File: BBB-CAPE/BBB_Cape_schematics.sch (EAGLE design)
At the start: 81 parts, among them IC1 EEPROM-I2CSMD, SW1 219-02, SW2 219-02

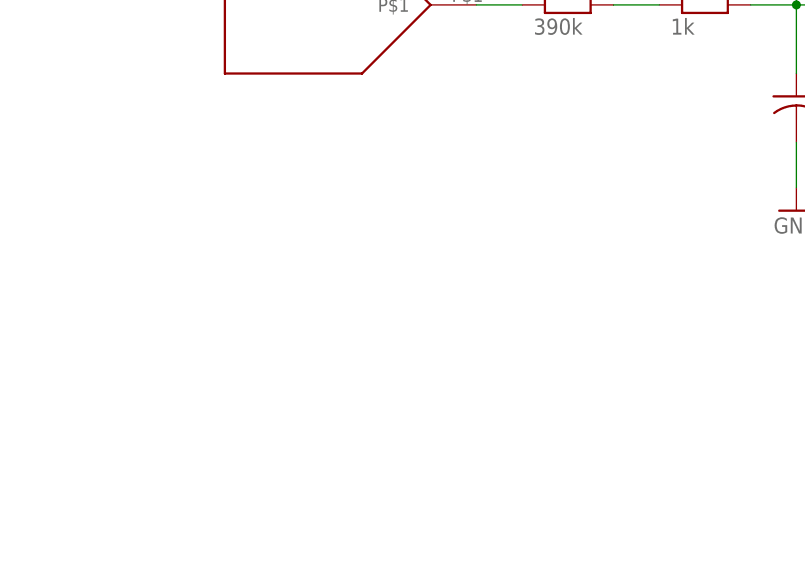
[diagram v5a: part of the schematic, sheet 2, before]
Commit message: Add ground pad(for index finger) in BBB_Cape_schematics.sch
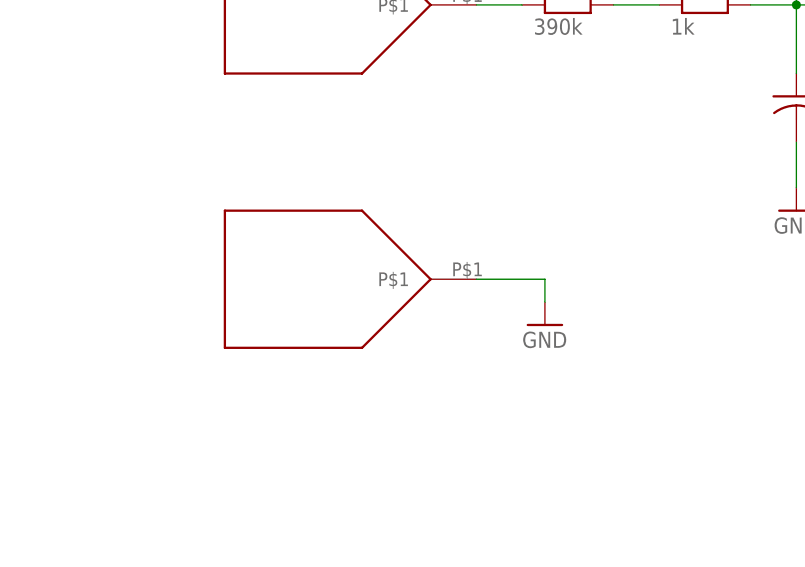
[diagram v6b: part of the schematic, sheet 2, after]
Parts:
- added U$24: PAD, Components:PAD
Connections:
- net GND: now also U$24.P$1
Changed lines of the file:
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@@
 <grid distance="0.1" unitdist="inch" unit="inch" style="lines" multiple="1" display="yes" altdistance="0.01" altunitdist="inch" altunit="inch"/>
 <layers>
-<layer number="1" name="Top" color="4" fill="1" visible="yes" active="no"/>
-<layer number="2" name="Route2" color="1" fill="3" visible="yes" active="no"/>
-<layer number="3" name="Route3" color="4" fill="3" visible="yes" active="no"/>
-<layer number="4" name="Route4" color="1" fill="4" visible="yes" active="no"/>
-<layer number="5" name="Route5" color="4" fill="4" visible="yes" active="no"/>
-<layer number="6" name="Route6" color="1" fill="8" visible="yes" active="no"/>
-<layer number="7" name="Route7" color="4" fill="8" visible="yes" active="no"/>
-<layer number="8" name="Route8" color="1" fill="2" visible="yes" active="no"/>
-<layer number="9" name="Route9" color="4" fill="2" visible="yes" active="no"/>
-<layer number="10" name="Route10" color="1" fill="7" visible="yes" active="no"/>
-<layer number="11" name="Route11" color="4" fill="7" visible="yes" active="no"/>
-<layer number="12" name="Route12" color="1" fill="5" visible="yes" active="no"/>
-<layer number="13" name="Route13" color="4" fill="5" visible="yes" active="no"/>
-<layer number="14" name="Route14" color="1" fill="6" visible="yes" active="no"/>
-<layer number="15" name="Route15" color="4" fill="6" visible="yes" active="no"/>
-<layer number="16" name="Bottom" color="1" fill="1" visible="yes" active="no"/>
-<layer number="17" name="Pads" color="2" fill="1" visible="yes" active="no"/>
-<layer number="18" name="Vias" color="2" fill="1" visible="yes" active="no"/>
-<layer number="19" name="Unrouted" color="6" fill="1" visible="yes" active="no"/>
-<layer number="20" name="Dimension" color="15" fill="1" visible="yes" active="no"/>
-<layer number="21" name="tPlace" color="7" fill="1" visible="yes" active="no"/>
-<layer number="22" name="bPlace" color="7" fill="1" visible="yes" active="no"/>
-<layer number="23" name="tOrigins" color="15" fill="1" visible="yes" active="no"/>
-<layer number="24" name="bOrigins" color="15" fill="1" visible="yes" active="no"/>
-<layer number="25" name="tNames" color="7" fill="1" visible="yes" active="no"/>
-<layer number="26" name="bNames" color="7" fill="1" visible="yes" active="no"/>
-<layer number="27" name="tValues" color="7" fill="1" visible="yes" active="no"/>
-<layer number="28" name="bValues" color="7" fill="1" visible="yes" active="no"/>
+<layer number="1" name="Top" color="4" fill="1" visible="no" active="no"/>
+<layer number="2" name="Route2" color="1" fill="3" visible="no" active="no"/>
+<layer number="3" name="Route3" color="4" fill="3" visible="no" active="no"/>
+<layer number="4" name="Route4" color="1" fill="4" visible="no" active="no"/>
+<layer number="5" name="Route5" color="4" fill="4" visible="no" active="no"/>
+<layer number="6" name="Route6" color="1" fill="8" visible="no" active="no"/>
+<layer number="7" name="Route7" color="4" fill="8" visible="no" active="no"/>
+<layer number="8" name="Route8" color="1" fill="2" visible="no" active="no"/>
+<layer number="9" name="Route9" color="4" fill="2" visible="no" active="no"/>
+<layer number="10" name="Route10" color="1" fill="7" visible="no" active="no"/>
+<layer number="11" name="Route11" color="4" fill="7" visible="no" active="no"/>
+<layer number="12" name="Route12" color="1" fill="5" visible="no" active="no"/>
+<layer number="13" name="Route13" color="4" fill="5" visible="no" active="no"/>
+<layer number="14" name="Route14" color="1" fill="6" visible="no" active="no"/>
+<layer number="15" name="Route15" color="4" fill="6" visible="no" active="no"/>
+<layer number="16" name="Bottom" color="1" fill="1" visible="no" active="no"/>
+<layer number="17" name="Pads" color="2" fill="1" visible="no" active="no"/>
+<layer number="18" name="Vias" color="2" fill="1" visible="no" active="no"/>
+<layer number="19" name="Unrouted" color="6" fill="1" visible="no" active="no"/>
+<layer number="20" name="Dimension" color="15" fill="1" visible="no" active="no"/>
+<layer number="21" name="tPlace" color="7" fill="1" visible="no" active="no"/>
+<layer number="22" name="bPlace" color="7" fill="1" visible="no" active="no"/>
+<layer number="23" name="tOrigins" color="15" fill="1" visible="no" active="no"/>
+<layer number="24" name="bOrigins" color="15" fill="1" visible="no" active="no"/>
+<layer number="25" name="tNames" color="7" fill="1" visible="no" active="no"/>
+<layer number="26" name="bNames" color="7" fill="1" visible="no" active="no"/>
+<layer number="27" name="tValues" color="7" fill="1" visible="no" active="no"/>
+<layer number="28" name="bValues" color="7" fill="1" visible="no" active="no"/>
 <layer number="29" name="tStop" color="7" fill="3" visible="no" active="no"/>
 <layer number="30" name="bStop" color="7" fill="6" visible="no" active="no"/>
@@
 <layer number="35" name="tGlue" color="7" fill="4" visible="no" active="no"/>
 <layer number="36" name="bGlue" color="7" fill="5" visible="no" active="no"/>
-<layer number="37" name="tTest" color="7" fill="1" visible="yes" active="no"/>
-<layer number="38" name="bTest" color="7" fill="1" visible="yes" active="no"/>
+<layer number="37" name="tTest" color="7" fill="1" visible="no" active="no"/>
+<layer number="38" name="bTest" color="7" fill="1" visible="no" active="no"/>
 <layer number="39" name="tKeepout" color="4" fill="11" visible="no" active="no"/>
 <layer number="40" name="bKeepout" color="1" fill="11" visible="no" active="no"/>
@@
 <layer number="44" name="Drills" color="7" fill="1" visible="no" active="no"/>
 <layer number="45" name="Holes" color="7" fill="1" visible="no" active="no"/>
-<layer number="46" name="Milling" color="3" fill="1" visible="yes" active="no"/>
-<layer number="47" name="Measures" color="7" fill="1" visible="yes" active="no"/>
-<layer number="48" name="Document" color="7" fill="1" visible="yes" active="no"/>
-<layer number="49" name="Reference" color="7" fill="1" visible="yes" active="no"/>
-<layer number="50" name="dxf" color="7" fill="1" visible="yes" active="no"/>
-<layer number="51" name="tDocu" color="7" fill="1" visible="yes" active="no"/>
-<layer number="52" name="bDocu" color="7" fill="1" visible="yes" active="no"/>
-<layer number="53" name="tGND_GNDA" color="7" fill="9" visible="yes" active="no"/>
-<layer number="54" name="bGND_GNDA" color="1" fill="9" visible="yes" active="no"/>
-<layer number="56" name="wert" color="7" fill="1" visible="yes" active="no"/>
+<layer number="46" name="Milling" color="3" fill="1" visible="no" active="no"/>
+<layer number="47" name="Measures" color="7" fill="1" visible="no" active="no"/>
+<layer number="48" name="Document" color="7" fill="1" visible="no" active="no"/>
+<layer number="49" name="Reference" color="7" fill="1" visible="no" active="no"/>
+<layer number="50" name="dxf" color="7" fill="1" visible="no" active="no"/>
+<layer number="51" name="tDocu" color="7" fill="1" visible="no" active="no"/>
+<layer number="52" name="bDocu" color="7" fill="1" visible="no" active="no"/>
+<layer number="53" name="tGND_GNDA" color="7" fill="9" visible="no" active="no"/>
+<layer number="54" name="bGND_GNDA" color="1" fill="9" visible="no" active="no"/>
+<layer number="56" name="wert" color="7" fill="1" visible="no" active="no"/>
 <layer number="91" name="Nets" color="2" fill="1" visible="yes" active="yes"/>
 <layer number="92" name="Busses" color="1" fill="1" visible="yes" active="yes"/>
@@
 <part name="SW1" library="switch-dil" deviceset="219-02*" device=""/>
 <part name="SW2" library="switch-dil" deviceset="219-02*" device=""/>
+<part name="U$24" library="Components" deviceset="PAD" device=""/>
+<part name="GND28" library="supply1" deviceset="GND" device=""/>
 </parts>
 <sheets>
@@
 <attribute name="VALUE" x="334.264" y="220.091" size="1.778" layer="96" rot="R180"/>
 </instance>
+<instance part="U$24" gate="G$1" x="68.58" y="139.7"/>
+<instance part="GND28" gate="1" x="93.98" y="134.62"/>
 </instances>
 <busses>
@@
 <wire x1="195.58" y1="137.16" x2="195.58" y2="134.62" width="0.1524" layer="91"/>
 </segment>
-</net>
+<segment>
+<pinref part="U$24" gate="G$1" pin="P$1"/>
+<wire x1="86.36" y1="139.7" x2="93.98" y2="139.7" width="0.1524" layer="91"/>
+<pinref part="GND28" gate="1" pin="GND"/>
+<wire x1="93.98" y1="139.7" x2="93.98" y2="137.16" width="0.1524" layer="91"/>
+</segment>
+</net>

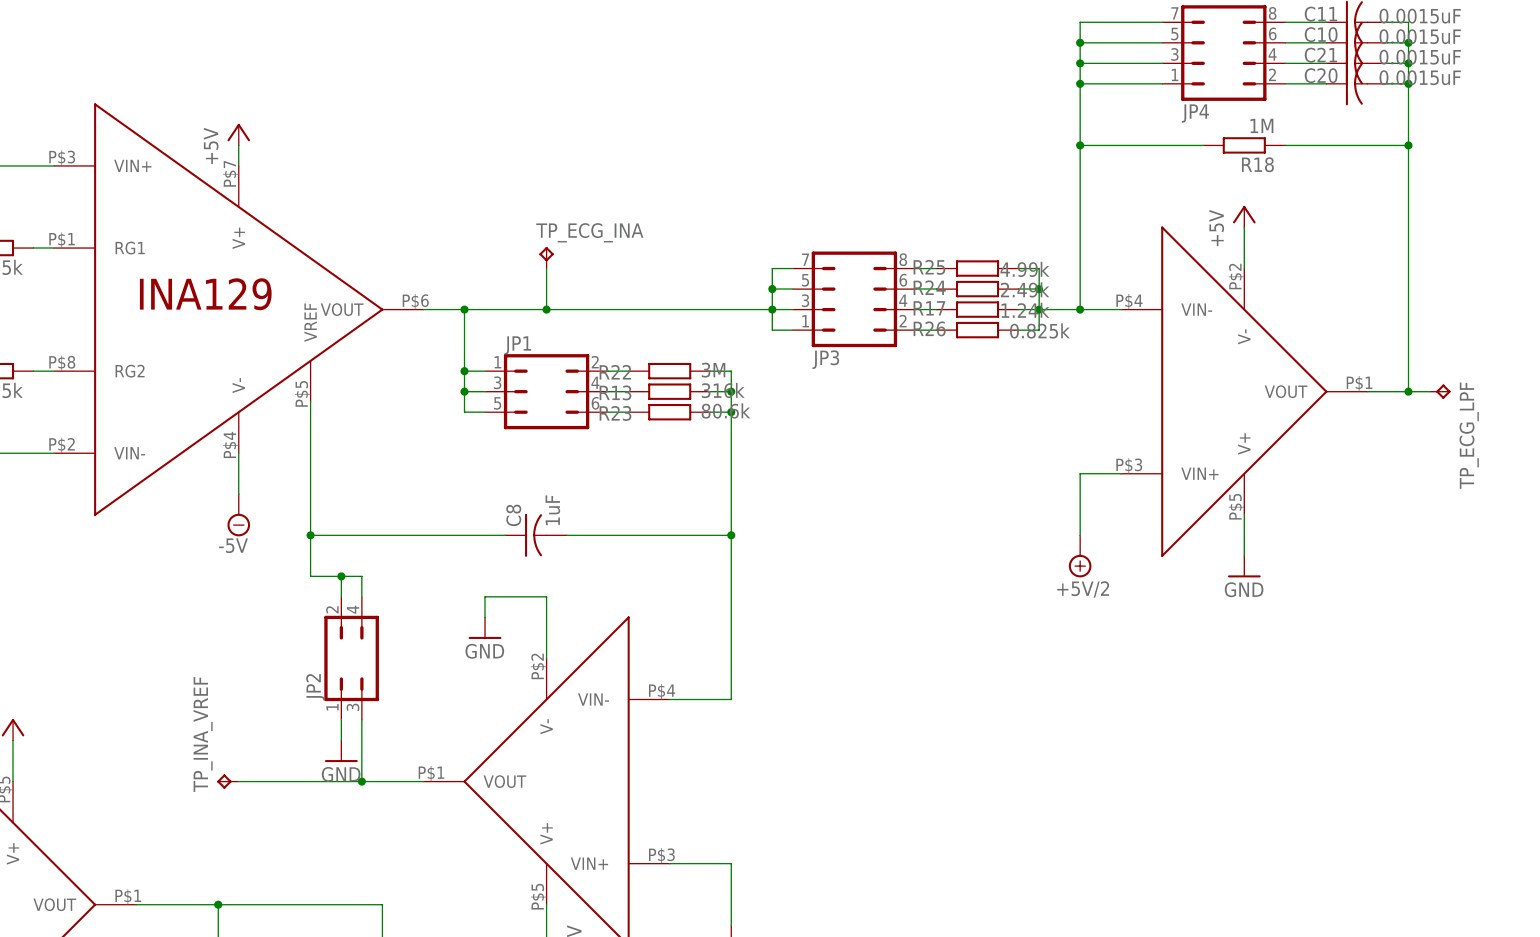
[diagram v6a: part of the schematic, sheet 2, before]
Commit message: Change layout of Crystal oscillator and rename OPA353 to OPA335 in Components.lbr. Replace OPA2021 with OPA335 in LPF design in BBB_Cape_schematics.sch
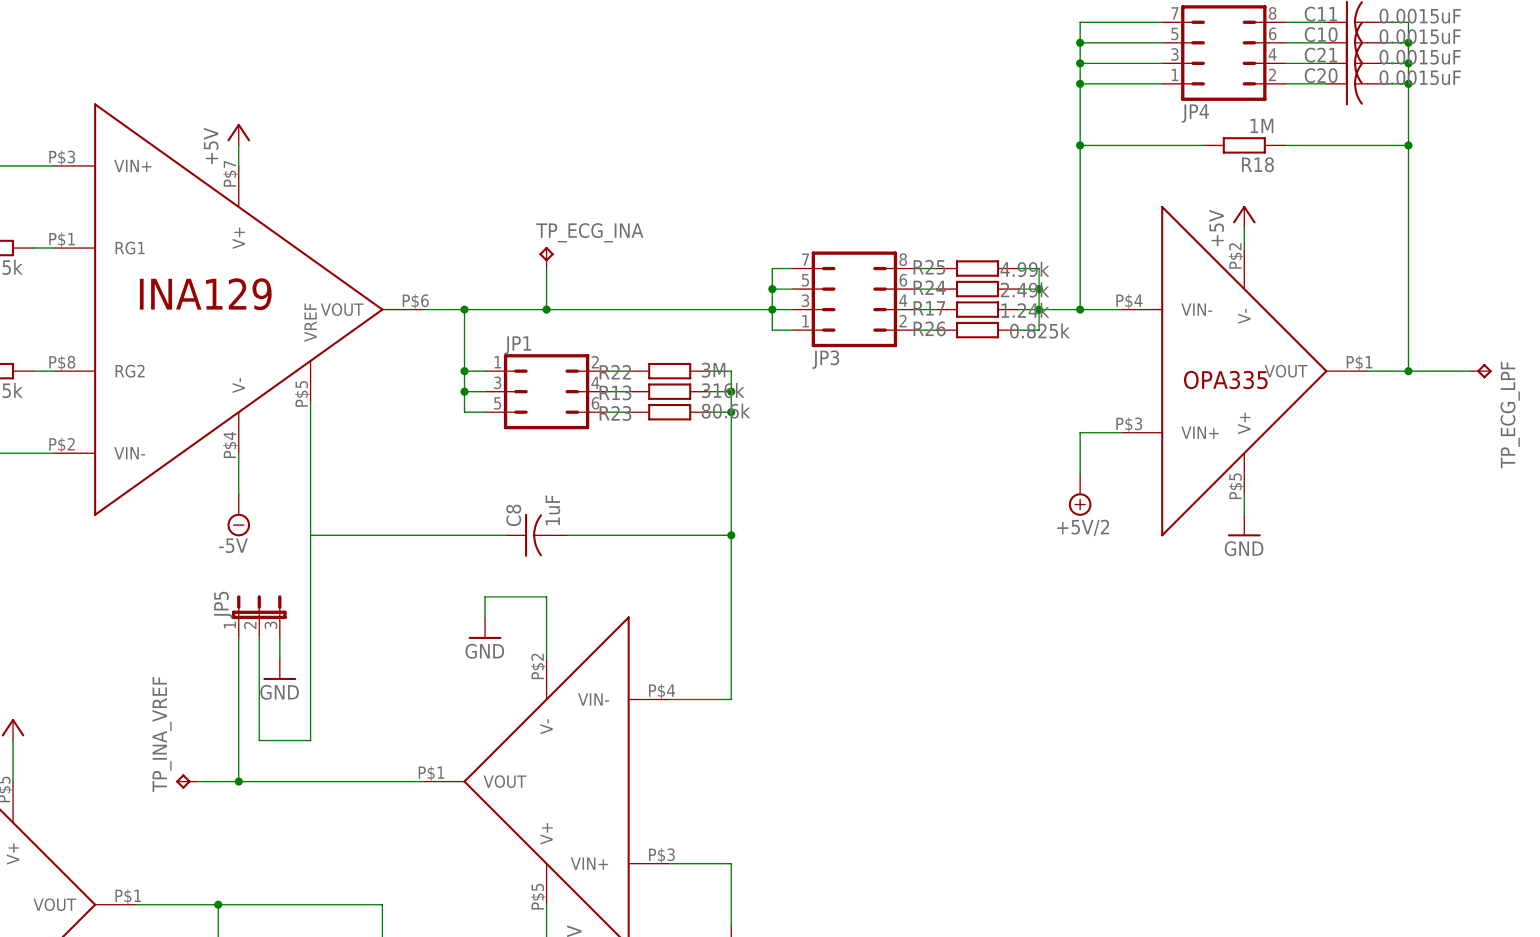
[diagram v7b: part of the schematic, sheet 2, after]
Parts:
- removed C17: 0.10uF, rcl:C-USC1206
- removed JP2: (no value), jumper:JP2Q
- removed SW1: 219-02, switch-dil:219-02
- added C12: 0.10uF, rcl:C-USC1206
- added JP5: (no value), jumper:JP2E
- U$13: value LMP2021 -> OPA335; device Components:LMP2021 -> Components:OPA335
- U$22: value OPA353 -> OPA335; device Components:OPA353 -> Components:OPA335
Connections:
- removed net N$36: BB1P9.3.3V@1, SW1.4
- removed net N$45: BB1P9.5V_RAW@1, SW1.3
- net +5V: now also C12.1, U$22.V+; no longer C17.1, U$22.V-
- net 3.3V: now also BB1P9.3.3V@1; no longer SW1.1
- net 5V: now also BB1P9.5V_RAW@1; no longer SW1.2
- net GND: now also C12.2, JP5.3, U$22.V-; no longer C17.2, JP2.1, U$22.V+
- net N$10: now also JP5.2; no longer JP2.2, JP2.4
- net N$35: now also JP5.1; no longer JP2.3
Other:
- moved on the sheet: TP_ECG_LPF, TP_INA_VREF
